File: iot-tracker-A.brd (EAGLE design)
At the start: 50.8 x 50.8 mm, 36 parts, among them J2 282834-2, Q1 MMBT3906, Q2 BSS138, U1 ESP-WROOM-02, U2 TPS61021ADSGR, U3 PCF85263ATL_AX, Y1 32.768kHz

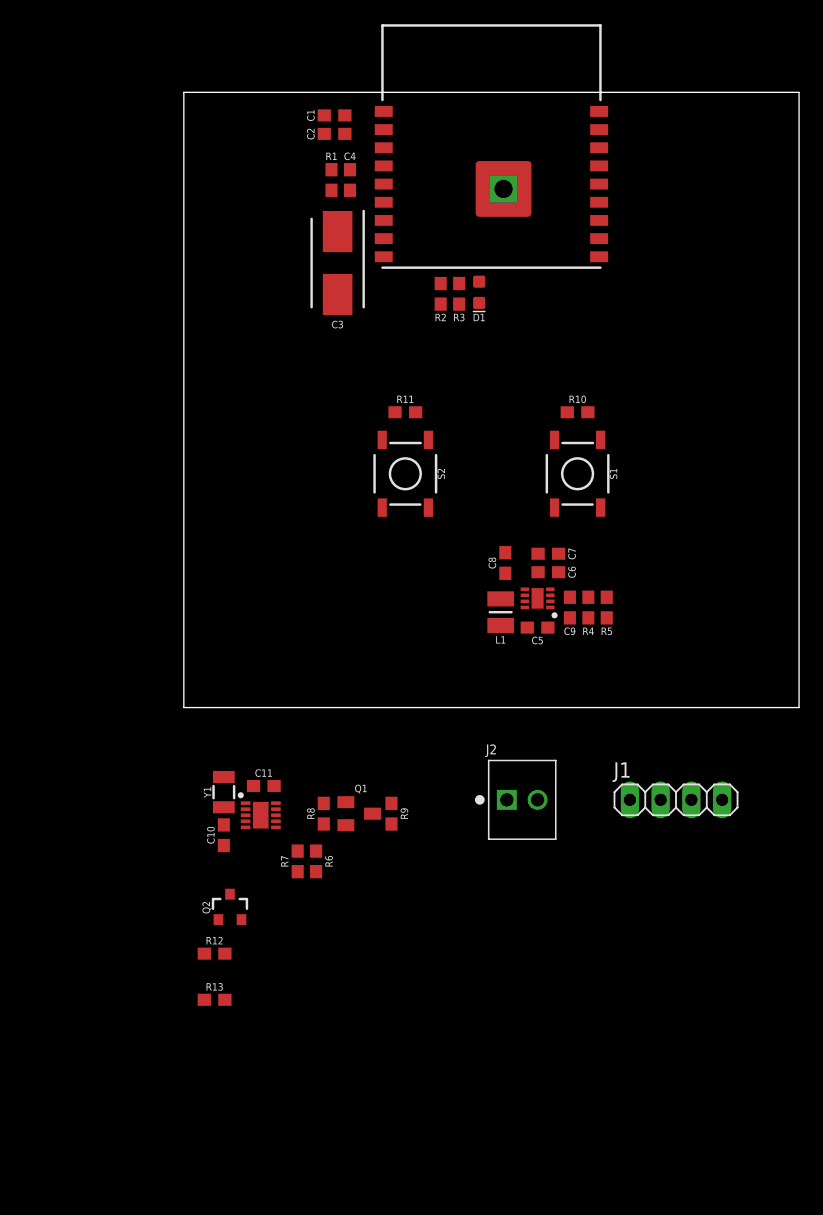
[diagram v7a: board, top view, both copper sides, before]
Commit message: Minor net fixes, partially routed every IC
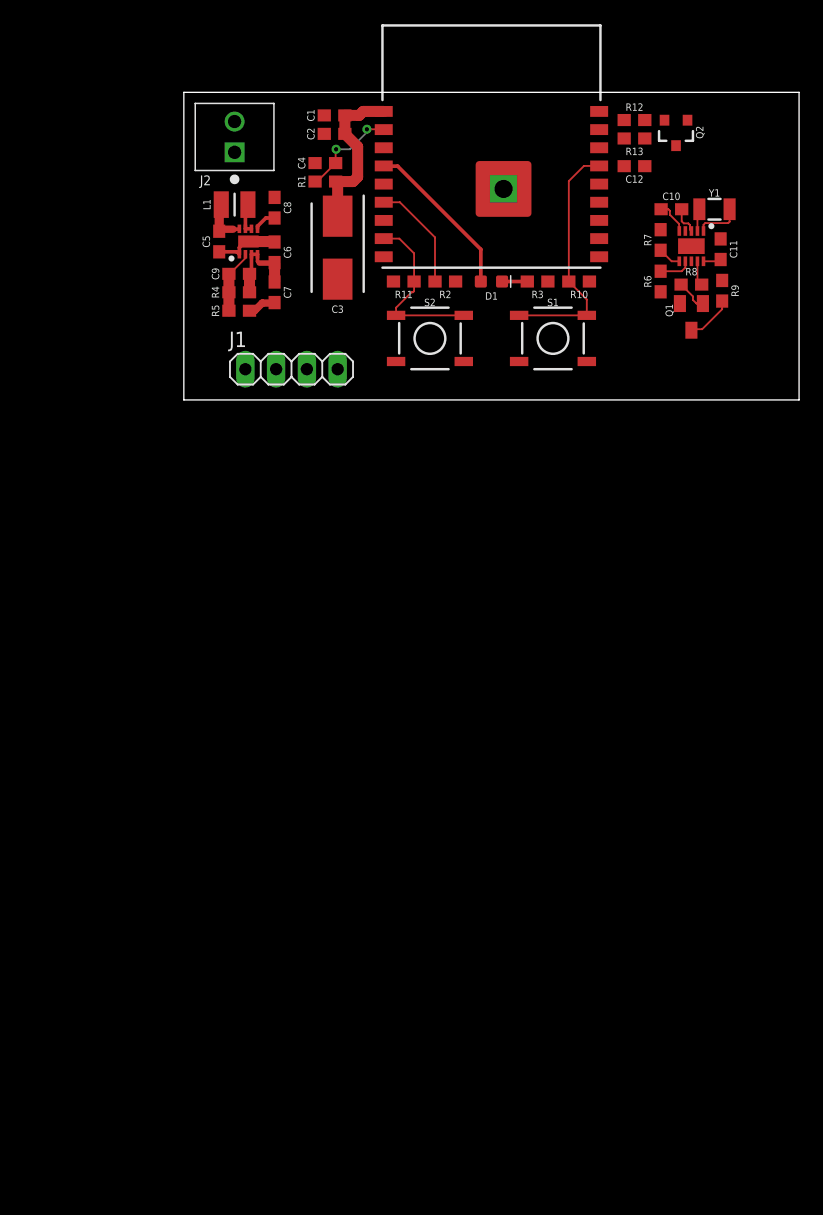
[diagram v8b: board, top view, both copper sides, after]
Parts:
- added C12: 0.1uF, SparkFun-Capacitors:0603
- moved R13 79.1 mm to (37.2, 47.0), turned to 180 degrees
- moved R12 77.1 mm to (37.2, 48.5)
- moved Q2 73.8 mm to (40.6, 47.5), turned to 180 degrees
- moved C10 63.5 mm to (40.3, 41.1), turned to 180 degrees
- moved Y1 62.9 mm to (43.8, 41.1), turned to 0 degrees
- moved J2 59.7 mm to (4.19, 47.1), turned to 90 degrees
- moved R7 59.4 mm to (39.4, 38.6), turned to 90 degrees
- moved U3 58.9 mm to (41.9, 38.1), turned to 270 degrees
- moved C11 58.2 mm to (44.3, 37.8), turned to 270 degrees
- moved R6 55.7 mm to (39.4, 35.2)
- moved R8 53.2 mm to (41.9, 34.9), turned to 180 degrees
- moved R9 51.1 mm to (44.5, 34.4), turned to 270 degrees
- moved Q1 49.3 mm to (41.9, 32.3), turned to 180 degrees
- moved J1 47.7 mm to (8.89, 27.9)
- moved C5 41.3 mm to (2.92, 38.5), turned to 270 degrees
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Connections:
- net INTA_PNP_B renamed PNP_B
- net N$1 renamed MOSFET_S
- net 3.3V: no longer J2.1
- net BOOT: now also S2.2
- net GND: now also C12.2, S1.4, S2.4
- net RST: now also C12.1, S1.2
- net V_BATT: now also J2.1
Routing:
- net 3.3V: track 0.00 -> 22.6 mm
- net RST: track 0.00 -> 20.3 mm
- net BOOT: track 0.00 -> 14.4 mm
- net IO12_LED: track 0.00 -> 13.5 mm
- net GND: track 0.00 -> 10.5 mm
- net IO15: track 0.00 -> 9.08 mm
- net ESP_EN: track 0.00 -> 8.27 mm, vias 0 -> 2
- net V_BATT: track 0.00 -> 6.65 mm
- net BOOST_EN: track 0.00 -> 5.83 mm
- net FB: track 0.00 -> 5.27 mm
- net OSCI: track 0.00 -> 3.81 mm
- net SCL: track 0.00 -> 2.68 mm
- net PNP_B: track 0.00 -> 2.62 mm
- net SW: track 0.00 -> 2.58 mm
- net LED_CATH: track 0.00 -> 2.08 mm
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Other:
- board size 50.8 x 50.8 mm -> 50.8 x 25.4 mm
